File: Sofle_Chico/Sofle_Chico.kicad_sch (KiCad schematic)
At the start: 120 parts, among them J1 Conn_01x05, J2 MJ-4PP-9, J3 Conn_01x04, J4 Conn_01x04, J5 Conn_01x05, J6 Conn_01x05, J7 Conn_01x04, Q1 DMG2305UX, SW1 SW_PUSH, SW10 SW_PUSH, SW11 SW_PUSH, SW12 SW_PUSH, SW13 SW_PUSH, SW14 SW_PUSH, SW15 SW_PUSH, SW16 SW_PUSH, SW17 SW_PUSH, SW18 SW_PUSH, SW19 SW_PUSH, SW2 SW_PUSH, SW20 SW_PUSH, SW21 SW_PUSH, SW22 SW_PUSH, SW23 SW_PUSH, SW24 SW_PUSH, SW25 Rotary_Encoder_Switch-Device, SW26 SW_PUSH, SW27 SW_PUSH, SW28 SW_PUSH, SW29 SW_PUSH, SW3 SW_PUSH, SW30 SW_PUSH, SW4 SW_PUSH, SW5 SW_PUSH, SW6 SW_PUSH, SW7 SW_PUSH, SW8 SW_PUSH, SW9 SW_PUSH, U1 SN74AHCT1G125, U2 Pico

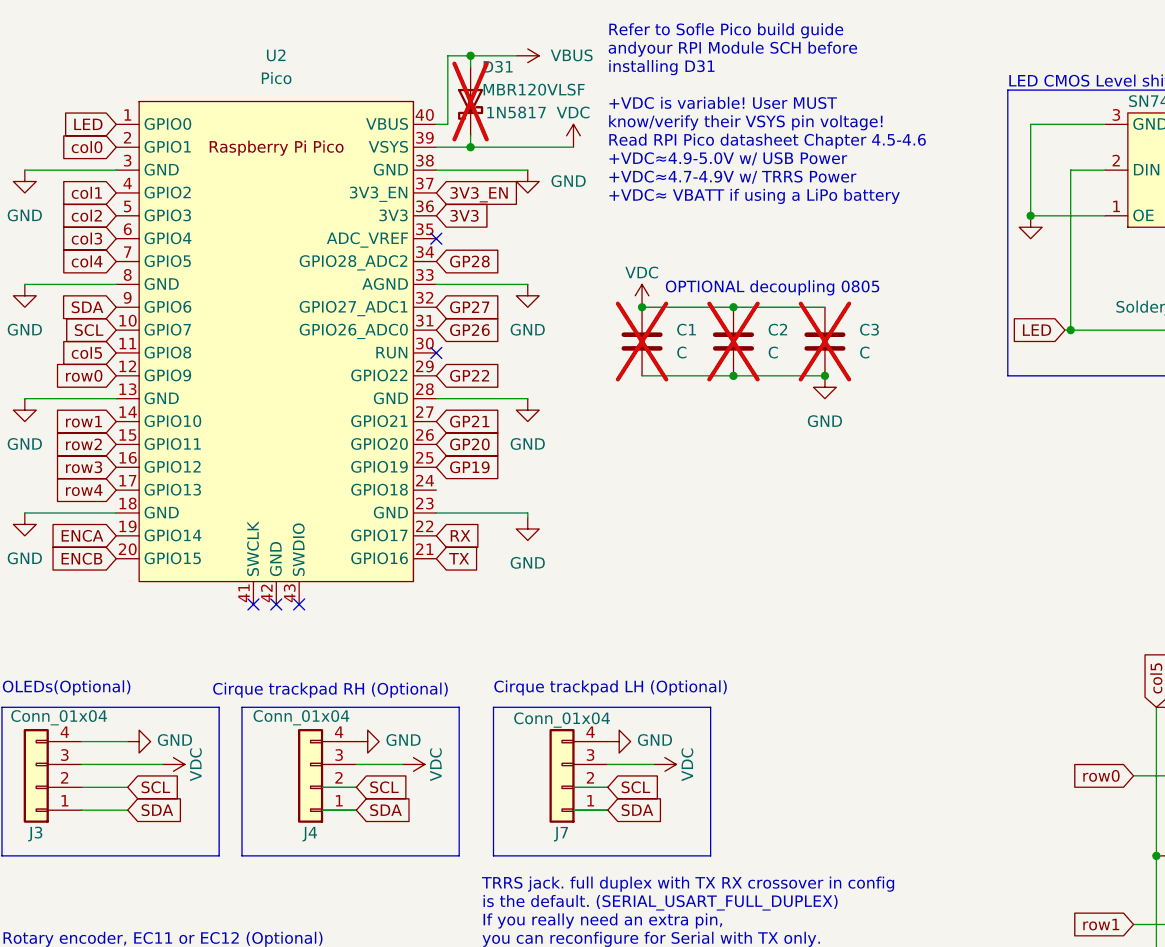
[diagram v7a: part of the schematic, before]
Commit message: Swapped peripheral headers to 3.3v from VSYS to prevent over-powering devices, OLED/cirque both 3.3V preferred
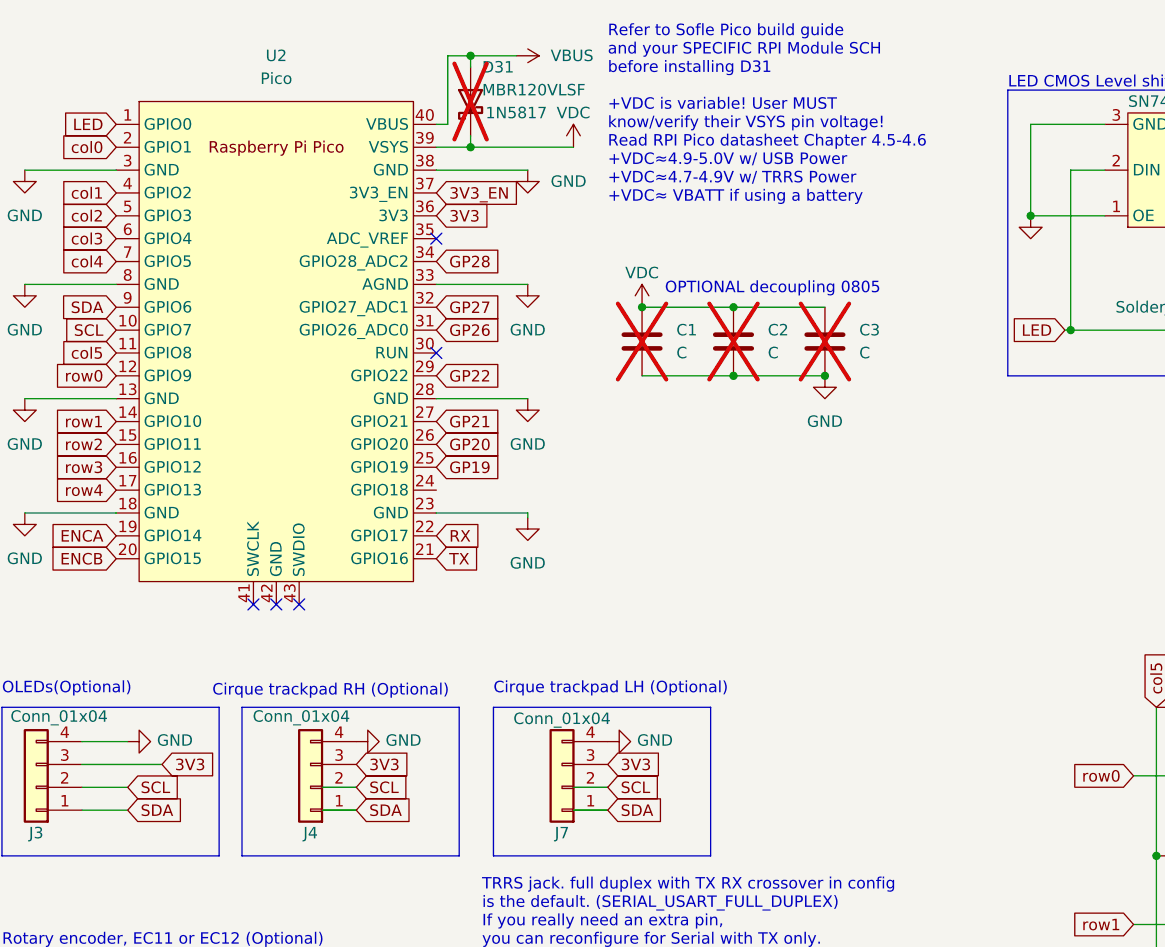
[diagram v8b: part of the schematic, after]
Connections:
- net 3V3: now also J3.3 (Pin_3), J4.3 (Pin_3), J7.3 (Pin_3)
- net VDC: no longer J3.3 (Pin_3), J4.3 (Pin_3), J7.3 (Pin_3)
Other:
- note added: "Refer to Sofle Pico build guide and your SPECIFIC RPI Module SCH before installing D31 +VDC is variable! User MUST know/verify their VSYS pin voltage! Read RPI Pico datasheet Chapter 4.5-4.6 +VDC≈4.9-5.0V w/ USB Power +VDC≈4.7-4.9V w/ TRRS Power +VDC≈ VBATT if using a battery"
- note removed: "Refer to Sofle Pico build guide andyour RPI Module SCH before installing D31 +VDC is variable! User MUST know/verify their VSYS pin voltage! Read RPI Pico datasheet Chapter 4.5-4.6 +VDC≈4.9-5.0V w/ USB Power +VDC≈4.7-4.9V w/ TRRS Power +VDC≈ VBATT if using a LiPo battery"
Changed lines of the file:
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@@
     (stroke (width 0) (type default))
   )
-  (wire (pts (xy 87.63 96.52) (xy 82.55 96.52))
-    (stroke (width 0) (type default))
-  )
   (wire (pts (xy 256.54 45.72) (xy 246.38 45.72))
     (stroke (width 0) (type default))
@@
     (stroke (width 0) (type default))
   )
-  (wire (pts (xy 59.69 96.52) (xy 54.61 96.52))
-    (stroke (width 0) (type default))
-  )
   (wire (pts (xy 170.18 76.2) (xy 172.72 76.2))
     (stroke (width 0) (type default))
@@
     (effects (font (size 1.27 1.27)) (justify left bottom))
   )
-  (text "Refer to Sofle Pico build guide \nandyour RPI Module SCH before \ninstalling D31\n\n+VDC is variable! User MUST\nknow/verify their VSYS pin voltage!\nRead RPI Pico datasheet Chapter 4.5-4.6\n+VDC≈4.9-5.0V w/ USB Power\n+VDC≈4.7-4.9V w/ TRRS Power\n+VDC≈ VBATT if using a LiPo battery"
+  (text "Refer to Sofle Pico build guide \nand your SPECIFIC RPI Module SCH \nbefore installing D31\n\n+VDC is variable! User MUST\nknow/verify their VSYS pin voltage!\nRead RPI Pico datasheet Chapter 4.5-4.6\n+VDC≈4.9-5.0V w/ USB Power\n+VDC≈4.7-4.9V w/ TRRS Power\n+VDC≈ VBATT if using a battery"
     (at 82.55 34.29 0)
     (effects (font (size 1.27 1.27)) (justify left bottom))
@@
     )
   )
+  (global_label "3V3" (shape input) (at 82.55 96.52 0) (fields_autoplaced)
+    (effects (font (size 1.27 1.27)) (justify left))
+    (property "Intersheetrefs" "${INTERSHEET_REFS}" (at 88.3092 96.52 0)
+      (effects (font (size 1.27 1.27)) (justify left) hide)
+    )
+  )
   (global_label "TX" (shape input) (at 63.5 73.66 0) (fields_autoplaced)
     (effects (font (size 1.27 1.27)) (justify left))
@@
     )
   )
+  (global_label "3V3" (shape input) (at 54.61 96.52 0) (fields_autoplaced)
+    (effects (font (size 1.27 1.27)) (justify left))
+    (property "Intersheetrefs" "${INTERSHEET_REFS}" (at 60.3692 96.52 0)
+      (effects (font (size 1.27 1.27)) (justify left) hide)
+    )
+  )
   (global_label "col3" (shape input) (at 184.15 90.17 90)
     (effects (font (size 1.27 1.27)) (justify left))
@@
     )
   )
+  (global_label "3V3" (shape input) (at 33.02 96.52 0) (fields_autoplaced)
+    (effects (font (size 1.27 1.27)) (justify left))
+    (property "Intersheetrefs" "${INTERSHEET_REFS}" (at 38.7792 96.52 0)
+      (effects (font (size 1.27 1.27)) (justify left) hide)
+    )
+  )
   (global_label "SCL" (shape input) (at 27.94 48.26 180) (fields_autoplaced)
     (effects (font (size 1.27 1.27)) (justify right))
@@
     )
   )
-  (symbol (lib_id "power:VDC") (at 33.02 96.52 270) (unit 1)
-    (in_bom yes) (on_board yes) (dnp no) (fields_autoplaced)
-    (property "Reference" "#PWR010" (at 29.21 96.52 0)
-      (effects (font (size 1.27 1.27)) hide)
-    )
-    (property "Value" "VDC" (at 36.83 96.52 0)
-      (effects (font (size 1.27 1.27)))
-    )
-    (property "Footprint" "" (at 33.02 96.52 0)
-      (effects (font (size 1.27 1.27)) hide)
-    )
-    (property "Datasheet" "" (at 33.02 96.52 0)
-      (effects (font (size 1.27 1.27)) hide)
-    )
-    (pin "1")
-    (instances
-      (project "Sofle_Chico"
-        (path "/06057b3a-55ab-4f4e-913e-2aeec5ff3587"
-          (reference "#PWR010") (unit 1)
-        )
-      )
-    )
-  )
   (symbol (lib_id "Sofle_Pico:Conn_01x04") (at 49.53 99.06 180) (unit 1)
     (in_bom yes) (on_board yes) (dnp no)
@@
     )
   )
-  (symbol (lib_id "power:VDC") (at 87.63 96.52 270) (unit 1)
-    (in_bom yes) (on_board yes) (dnp no) (fields_autoplaced)
-    (property "Reference" "#PWR020" (at 83.82 96.52 0)
-      (effects (font (size 1.27 1.27)) hide)
-    )
-    (property "Value" "VDC" (at 91.44 96.52 0)
-      (effects (font (size 1.27 1.27)))
-    )
-    (property "Footprint" "" (at 87.63 96.52 0)
-      (effects (font (size 1.27 1.27)) hide)
-    )
-    (property "Datasheet" "" (at 87.63 96.52 0)
-      (effects (font (size 1.27 1.27)) hide)
-    )
-    (pin "1")
-    (instances
-      (project "Sofle_Chico"
-        (path "/06057b3a-55ab-4f4e-913e-2aeec5ff3587"
-          (reference "#PWR020") (unit 1)
-        )
-      )
-    )
-  )
   (symbol (lib_id "Sofle_Pico:SN74AHCT1G125") (at 147.955 30.48 0) (mirror x) (unit 1)
     (in_bom yes) (on_board yes) (dnp no)
@@
         )
       )
-    )
-  )
-  (symbol (lib_id "power:VDC") (at 59.69 96.52 270) (unit 1)
-    (in_bom yes) (on_board yes) (dnp no) (fields_autoplaced)
-    (property "Reference" "#PWR013" (at 55.88 96.52 0)
-      (effects (font (size 1.27 1.27)) hide)
-    )
-    (property "Value" "VDC" (at 63.5 96.52 0)
-      (effects (font (size 1.27 1.27)))
-    )
-    (property "Footprint" "" (at 59.69 96.52 0)
-      (effects (font (size 1.27 1.27)) hide)
-    )
-    (property "Datasheet" "" (at 59.69 96.52 0)
-      (effects (font (size 1.27 1.27)) hide)
-    )
-    (pin "1")
-    (instances
-      (project "Sofle_Chico"
-        (path "/06057b3a-55ab-4f4e-913e-2aeec5ff3587"
-          (reference "#PWR013") (unit 1)
-        )
-      )
